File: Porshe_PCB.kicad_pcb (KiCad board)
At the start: 2 copper layers, 80 x 80 mm, 44 parts, among them IC2 BH1750FVI-TR, J1 TF-115, J10 Conn_01x01_Pin, J11 Conn_01x01_Pin, J12 Conn_01x01_Pin, J14 Conn_02x20_Odd_Even, J16 Conn_02x20_Odd_Even, J2 SM04B-SRSS-TB_LF__SN_, J3 Conn_02x02_Odd_Even, J4 S2B-PH-SM4-TB_LF__SN_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

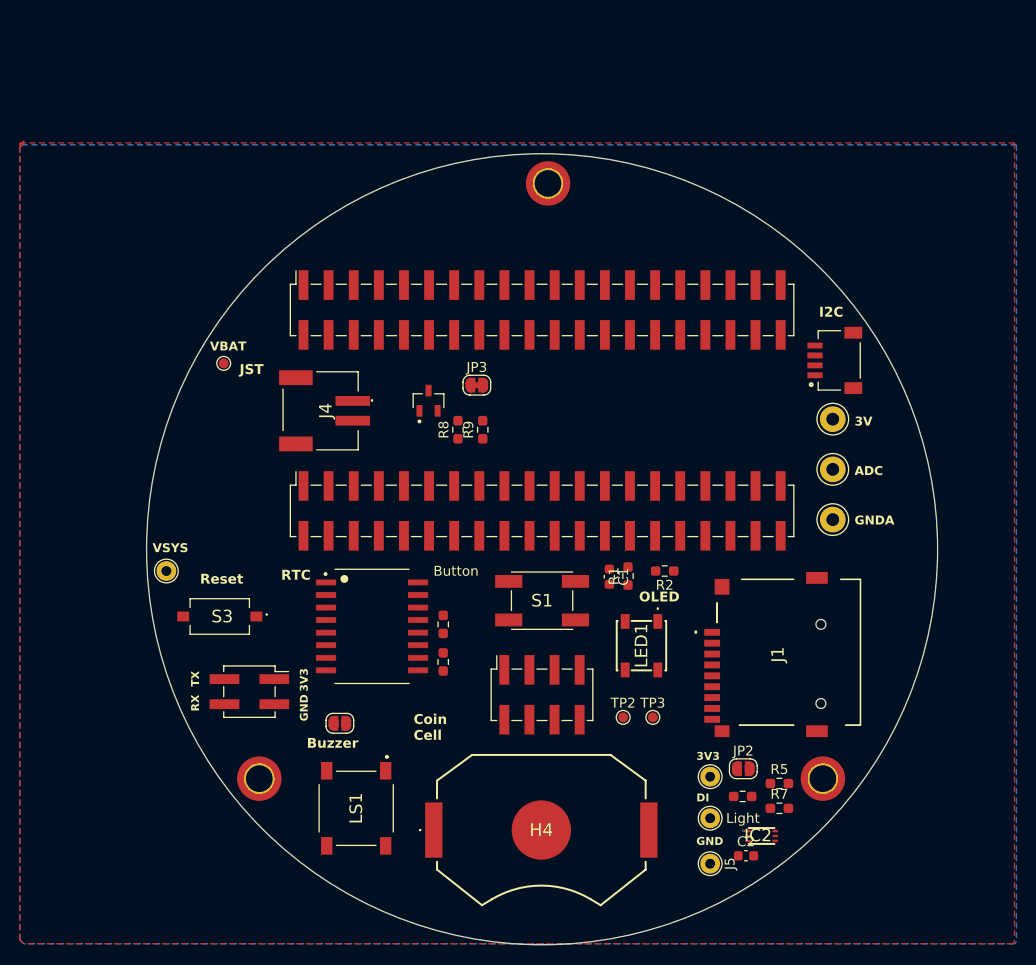
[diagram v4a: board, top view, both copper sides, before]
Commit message: add smartfarm function
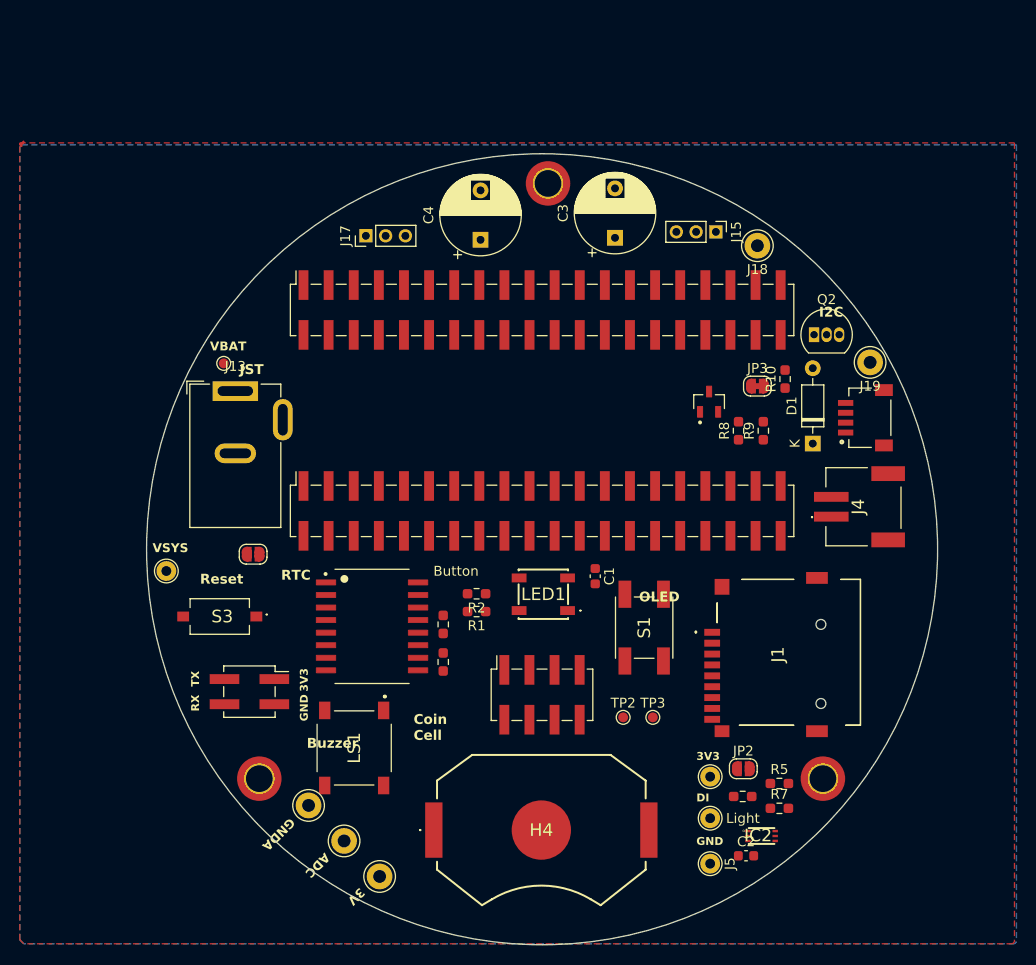
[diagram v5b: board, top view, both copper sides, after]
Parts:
- added C3: 1000uF/6.3V, Capacitor_THT:CP_Radial_D8.0mm_P5.00mm, F.Cu at (140.0, 67.0)
- added C4: 1000uF/6.3V, Capacitor_THT:CP_Radial_D8.0mm_P5.00mm, F.Cu at (126.4, 67.2)
- added D1: 1N5712, Diode_THT:D_DO-35_SOD27_P7.62mm_Horizontal, F.Cu at (160.0, 87.8)
- added J13: Barrel_Jack, Connector_BarrelJack:BarrelJack_GCT_DCJ200-10-A_Horizontal, F.Cu at (101.6, 82.5)
- added J15: Conn_01x03_Pin, Connector_PinHeader_2.00mm:PinHeader_1x03_P2.00mm_Vertical, F.Cu at (150.2, 66.4)
- added J17: Conn_01x03_Pin, Connector_PinHeader_2.00mm:PinHeader_1x03_P2.00mm_Vertical, F.Cu at (114.8, 66.8)
- added J18: Conn_01x01_Pin, Connector_Pin:Pin_D1.3mm_L11.0mm, F.Cu at (154.4, 67.8)
- added J19: Conn_01x01_Pin, Connector_Pin:Pin_D1.3mm_L11.0mm, F.Cu at (165.8, 79.6)
- added Q2: 2N3904, Package_TO_SOT_THT:TO-92_Inline, F.Cu at (160.1, 76.8)
- added R10: 1k, Resistor_SMD:R_0603_1608Metric_Pad0.98x0.95mm_HandSolder, F.Cu at (157.2, 81.3)
- R8, R9: value 10k -> 10k/1%
- moved J8 65.1 mm to (116.2, 131.6), turned to 45 degrees
- moved J6 62.1 mm to (112.6, 128.0), turned to 45 degrees
- moved J7 60.4 mm to (109.0, 124.4), turned to 45 degrees
- moved J4 55.8 mm to (165.1, 94.2), turned to -90 degrees
- moved R8 28.4 mm to (152.5, 86.5)
- moved JP3 28.4 mm to (154.4, 82.0)
- moved R9 28.4 mm to (155.0, 86.5)
- moved Q1 28.4 mm to (149.5, 83.6)
- moved JP1 19.2 mm to (103.4, 99.0)
- moved R2 19.2 mm to (126.0, 103.0)
- moved R1 15.7 mm to (126.0, 104.8), turned to 180 degrees
- moved LED1 11.2 mm to (132.8, 103.0), turned to 180 degrees
- moved S1 10.7 mm to (142.9, 106.4), turned to -90 degrees
- moved J2 6.58 mm to (163.3, 85.2)
- moved LS1 6.11 mm to (113.6, 118.6)
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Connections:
- net Net-(J14-Pin_27) renamed /DIN_2
- net Net-(J14-Pin_31) renamed /DIN_1
- net Net-(J14-Pin_33) renamed /FAN

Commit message: 첫번째 완성
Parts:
- added G***: LOGO, SmartFarm:DataPi_gondo, B.Cu at (132.6, 106.1)
- added R11: 220, Resistor_SMD:R_0603_1608Metric_Pad0.98x0.95mm_HandSolder, F.Cu at (149.1, 63.7)
- added R12: 220, Resistor_SMD:R_0603_1608Metric_Pad0.98x0.95mm_HandSolder, F.Cu at (117.9, 63.0)
- moved R6 66.6 mm to (95.3, 90.1), turned to -90 degrees
- moved J11 64.2 mm to (98.0, 87.6)
- moved J5 64.2 mm to (98.0, 92.2)
- moved J10 64.2 mm to (98.0, 83.4)
- moved J18 43.7 mm to (110.7, 67.6)
- moved Q1 39.7 mm to (109.8, 82.4), turned to 0 degrees
- moved D1 37.3 mm to (129.3, 66.7), turned to 0 degrees
- moved TP2 28.5 mm to (168.3, 108.3), turned to -90 degrees
- moved JP3 25.2 mm to (129.2, 81.2), turned to 180 degrees
- moved TP3 25.0 mm to (168.3, 110.7), turned to -90 degrees
- moved J13 24.9 mm to (112.5, 104.9), turned to -90 degrees
- moved J12 24.6 mm to (101.3, 77.0)
- moved R9 23.3 mm to (132.7, 79.9), turned to 0 degrees
- moved S3 21.0 mm to (103.2, 84.5), turned to -90 degrees
- moved R8 20.2 mm to (132.7, 82.4), turned to 0 degrees
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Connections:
- net /SPI0_MISO renamed /SPI1_MISO
- net /SPI0_MOSI renamed /SPI1_MOSI
- net /SPI_SC renamed /SPI1_SC
- C3 pad 1: Net-(J15-Pin_3) -> /VSYS
- C4 pad 1: Net-(J17-Pin_3) -> /VSYS
- J1 pad 5: /SPI0_SCK -> /SPI1_SCK
- J15 pad 1: /3V3 -> GND
- J15 pad 2: /DIN_1 -> Net-(J15-Pin_2)
- J15 pad 3: Net-(J15-Pin_3) -> /VSYS
- J17 pad 1: /3V3 -> GND
- J17 pad 2: /DIN_2 -> Net-(J17-Pin_2)
- J17 pad 3: Net-(J17-Pin_3) -> /VSYS
- LED1 pad 1: /3V3 -> /VSYS
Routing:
- net /3V3: track 0.00 -> 282.0 mm, vias 0 -> 11
- net /SDA: track 0.00 -> 122.9 mm
- net /SCL: track 0.00 -> 116.4 mm, vias 0 -> 2
- net /VSYS: track 0.00 -> 113.8 mm, vias 0 -> 2
- net /VBAT(+): track 0.00 -> 96.6 mm, vias 0 -> 4
- net /LED: track 0.00 -> 87.0 mm, vias 0 -> 2
- net GNDA: track 0.00 -> 85.2 mm, vias 0 -> 1
- net /ADC2: track 0.00 -> 84.9 mm, vias 0 -> 1
- net /RTC_RST: track 0.00 -> 73.8 mm
- net /BAK_VBAT: track 0.00 -> 64.3 mm
- net GND: track 0.00 -> 63.9 mm, vias 0 -> 35
- net /SW1: track 0.00 -> 58.6 mm
- net /DI: track 0.00 -> 53.5 mm, vias 0 -> 2
- net /RUN: track 0.00 -> 51.9 mm
- net /Buzz: track 0.00 -> 42.7 mm, vias 0 -> 2
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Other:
- board size 80 x 80 mm -> 79.1 x 80 mm
- board text added: "DIN"
- board text added: "SDcard"
- board text added: "VCC"

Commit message: 오토라우딩하기전
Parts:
- removed H1: MountingHole_Pad, MountingHole:MountingHole_2.7mm_M2.5_ISO7380_Pad_TopOnly
- removed J3: Conn_02x02_Odd_Even, Connector_PinSocket_2.54mm:PinSocket_2x02_P2.54mm_Vertical_SMD
- added H5: MountingHole_Pad, MountingHole:MountingHole_2.7mm_M2.5_ISO7380_Pad_TopOnly, F.Cu at (157.8, 63.8)
- added H6: MountingHole_Pad, MountingHole:MountingHole_2.7mm_M2.5_ISO7380_Pad_TopOnly, F.Cu at (155.8, 119.8)
- moved J7 79.8 mm to (165.7, 72.1), turned to -35 degrees
- moved J6 75.9 mm to (165.7, 76.3), turned to -35 degrees
- moved J8 72.1 mm to (165.7, 80.5), turned to -35 degrees
- moved J19 64.6 mm to (127.0, 126.0)
- moved C3 62.2 mm to (113.1, 121.7), turned to 0 degrees
- moved R11 60.7 mm to (110.0, 110.2), turned to -90 degrees
- moved J18 59.2 mm to (120.5, 126.0)
- moved Q2 57.9 mm to (122.2, 117.5), turned to 0 degrees
- moved H2 57.2 mm to (107.2, 64.6), turned to -90 degrees
- moved J15 56.1 mm to (116.4, 110.2)
- moved D1 54.4 mm to (123.8, 120.8), turned to -90 degrees
- moved R12 53.0 mm to (111.4, 115.6), turned to 90 degrees
- moved H3 52.3 mm to (108.8, 119.4), turned to -90 degrees
- moved J13 52.2 mm to (158.8, 80.7), turned to 180 degrees
- moved C4 49.7 mm to (107.5, 113.3), turned to 180 degrees
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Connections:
- J1 pad 1: /SPI1_SC -> /SPI0_SC
- J1 pad 3: /SPI1_MOSI -> /SPI0_MOSI
- J1 pad 5: /SPI1_SCK -> /SPI0_SCK
- J1 pad 7: /SPI1_MISO -> /SPI0_MISO
- J14 pad 19: Net-(J14-Pin_19) -> /DI
- J14 pad 20: Net-(J14-Pin_19) -> /DI
- J14 pad 23: /RTC_RST -> /Buzz
- J14 pad 24: /RTC_RST -> /Buzz
- J14 pad 27: /DIN_2 -> /LED
- J14 pad 28: /DIN_2 -> /LED
- J14 pad 29: Net-(J14-Pin_29) -> /SW1
- J14 pad 30: Net-(J14-Pin_29) -> /SW1
- J14 pad 31: /DIN_1 -> /SPI0_MOSI
- J14 pad 32: /DIN_1 -> /SPI0_MOSI
- J14 pad 33: /FAN -> /SPI0_SCK
- J14 pad 34: /FAN -> /SPI0_SCK
- J14 pad 37: Net-(J14-Pin_37) -> /SPI0_SC
- J14 pad 38: Net-(J14-Pin_37) -> /SPI0_SC
- J14 pad 39: Net-(J14-Pin_39) -> /SPI0_MISO
- J14 pad 40: Net-(J14-Pin_39) -> /SPI0_MISO
- J16 pad 19: /Buzz -> /RTC_RST
- J16 pad 20: /Buzz -> /RTC_RST
- J16 pad 21: /SPI1_MISO -> Net-(J16-Pin_21)
- J16 pad 22: /SPI1_MISO -> Net-(J16-Pin_21)
- J16 pad 23: /SPI1_SC -> Net-(J16-Pin_23)
- J16 pad 24: /SPI1_SC -> Net-(J16-Pin_23)
- J16 pad 27: /SPI1_SCK -> Net-(J16-Pin_27)
- J16 pad 28: /SPI1_SCK -> Net-(J16-Pin_27)
- J16 pad 29: /SPI1_MOSI -> Net-(J16-Pin_29)
- J16 pad 30: /SPI1_MOSI -> Net-(J16-Pin_29)
- J16 pad 33: /LED -> /FAN
- J16 pad 34: /LED -> /FAN
- J16 pad 37: /SW1 -> /DIN_1
- J16 pad 38: /SW1 -> /DIN_1
- J16 pad 39: Net-(J16-Pin_39) -> /DIN_2
- J16 pad 40: Net-(J16-Pin_39) -> /DIN_2
- R2 pad 1: /SPI1_SC -> /SPI0_SC
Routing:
- net /LED: track 87.0 -> 0.00 mm, vias 2 -> 0
- net /RTC_RST: track 73.8 -> 0.00 mm
- net /3V3: track 282.0 -> 211.4 mm, vias 11 -> 5
- net GND: track 63.9 -> 0.00 mm, vias 35 -> 0
- net GNDA: track 85.2 -> 23.3 mm, vias 1 -> 0
- net /VBAT(+): track 96.6 -> 35.2 mm, vias 4 -> 2
- net /SW1: track 58.6 -> 0.00 mm
- net /ADC2: track 84.9 -> 27.8 mm, vias 1 -> 2
- net /DI: track 53.5 -> 0.00 mm, vias 2 -> 0
- net /RUN: track 51.9 -> 0.00 mm
- net /SDA: track 122.9 -> 75.3 mm, vias 0 -> 2
- net /VSYS: track 113.8 -> 161.1 mm, vias 2 -> 4
- net /SCL: track 116.4 -> 71.8 mm, vias 2 -> 4
- net /Buzz: track 42.7 -> 0.00 mm, vias 2 -> 0
- net /Light_RST: track 41.5 -> 0.00 mm, vias 2 -> 0
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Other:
- board size 79.1 x 80 mm -> 80 x 79.1 mm
- board text added: "GP0"
- board text added: "GP0 GP1 GP2 GP3 GP4 GP5 GP6 GP7 GP8 GP9 GP10 GP11 GP12 GP13 GP14 GP15"
- board text added: "VBUS VSYS 3V3_EN 3V3 ADC_VREF GP28 GP27 GP26 RUN GP22 GP21 GP20 GP19 GP18 GP17 GP16"
- board text removed: "RX"
- board text removed: "TX"

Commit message: 주문을 위한 버전
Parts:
- moved TP2 14.9 mm to (171.2, 88.9)
- moved TP3 12.0 mm to (171.2, 93.3)
- moved R5 7.16 mm to (119.2, 107.8), turned to 0 degrees
- moved G*** 6.69 mm to (133.4, 108.0)
- moved LED1 6.38 mm to (163.8, 105.0), turned to 180 degrees
- moved J10 4.95 mm to (132.8, 90.4)
- moved R11 4.28 mm to (108.4, 106.2), turned to 0 degrees
- moved C4 4.24 mm to (105.1, 109.8)
- moved R12 4.23 mm to (107.8, 113.3), turned to -90 degrees
- moved S1 3.69 mm to (155.3, 109.7), turned to 90 degrees
- moved J17 3.31 mm to (111.5, 113.5)
- moved C1 2.99 mm to (160.2, 113.9)
- moved JP2 2.71 mm to (124.8, 112.7), turned to 180 degrees
- moved J15 2.67 mm to (114.3, 108.6)
- moved H6 2.20 mm to (157.4, 118.4)
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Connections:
- J16 pad 17: /DI -> Net-(J16-Pin_17)
- J16 pad 18: /DI -> Net-(J16-Pin_17)
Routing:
- net /Buzz: track 0.00 -> 55.0 mm, vias 0 -> 2
- net /SPI0_SC: track 24.0 -> 69.7 mm, vias 2 -> 3
- net /SW1: track 0.00 -> 43.2 mm, vias 0 -> 2
- net /RUN: track 0.00 -> 42.0 mm, vias 0 -> 2
- net /VSYS: track 161.1 -> 199.8 mm, vias 4 -> 3
- net /RTC_RST: track 0.00 -> 37.4 mm, vias 0 -> 2
- net /FAN: track 0.00 -> 37.3 mm, vias 0 -> 2
- net /LED: track 0.00 -> 33.5 mm, vias 0 -> 2
- net /Light_RST: track 0.00 -> 33.0 mm, vias 0 -> 2
- net /VBAT(+): track 35.2 -> 64.1 mm
- net /DI: track 0.00 -> 28.8 mm
- net Net-(J1-CD/DAT3): track 0.00 -> 26.7 mm, vias 0 -> 2
- net Net-(J1-DAT1): track 0.00 -> 23.2 mm, vias 0 -> 2
- net /DIN_2: track 0.00 -> 23.2 mm
- net /DIN_1: track 0.00 -> 20.3 mm
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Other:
- outline, holes or cut-outs redrawn
- board text added: "+"
- board text added: "-"
- board text added: "SCL"
- board text added: "SDA"
- board text added: "VBUS VSYS 3V3_EN 3V3 VREF GP28 GP27 GP26 RUN GP22 GP21 GP20 GP19 GP18 GP17 GP16"
- board text removed: "VBUS VSYS 3V3_EN 3V3 ADC_VREF GP28 GP27 GP26 RUN GP22 GP21 GP20 GP19 GP18 GP17 GP16"
